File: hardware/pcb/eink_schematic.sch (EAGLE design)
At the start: 0 parts

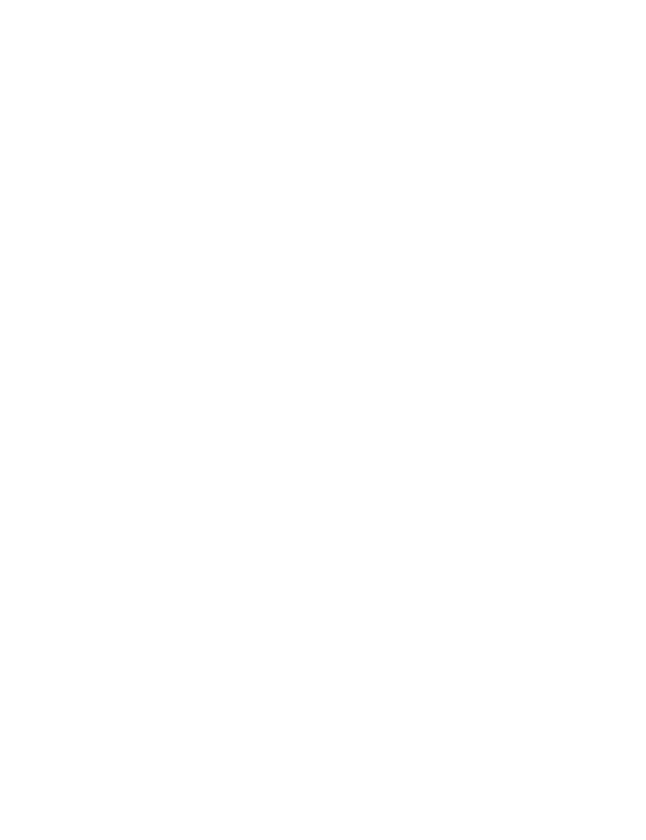
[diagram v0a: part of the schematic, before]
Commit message: rev78: just try writing text
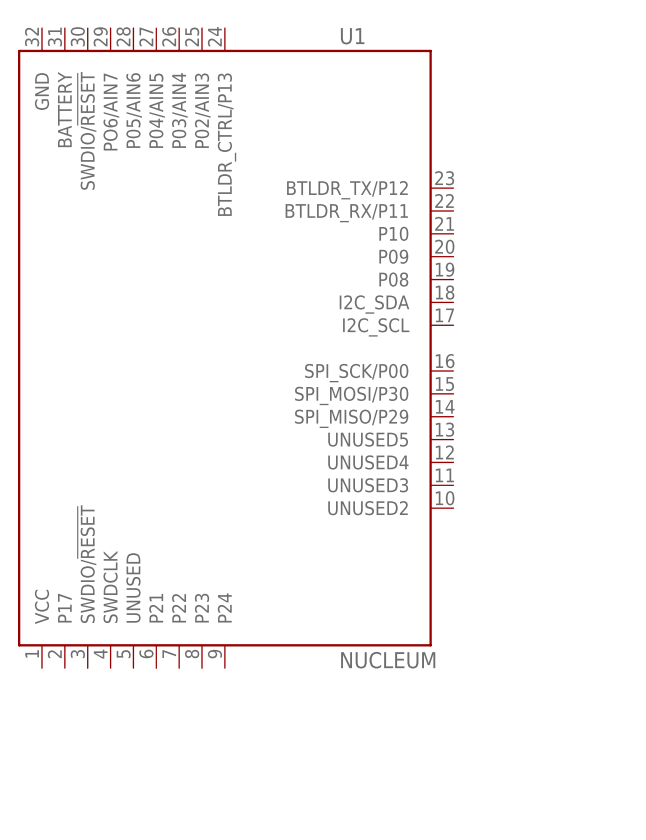
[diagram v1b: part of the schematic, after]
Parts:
- added U1: NUCLEUM, nucleum:NUCLEUM
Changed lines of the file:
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@@
 <parts>
 <part name="FRAME1" library="frames" deviceset="LETTER_L" device=""/>
+<part name="U1" library="nucleum" deviceset="NUCLEUM" device=""/>
 </parts>
 <sheets>
@@
 <instance part="FRAME1" gate="G$1" x="0" y="0"/>
 <instance part="FRAME1" gate="G$2" x="147.32" y="0"/>
+<instance part="U1" gate="G$1" x="127" y="101.6"/>
 </instances>
 <busses>

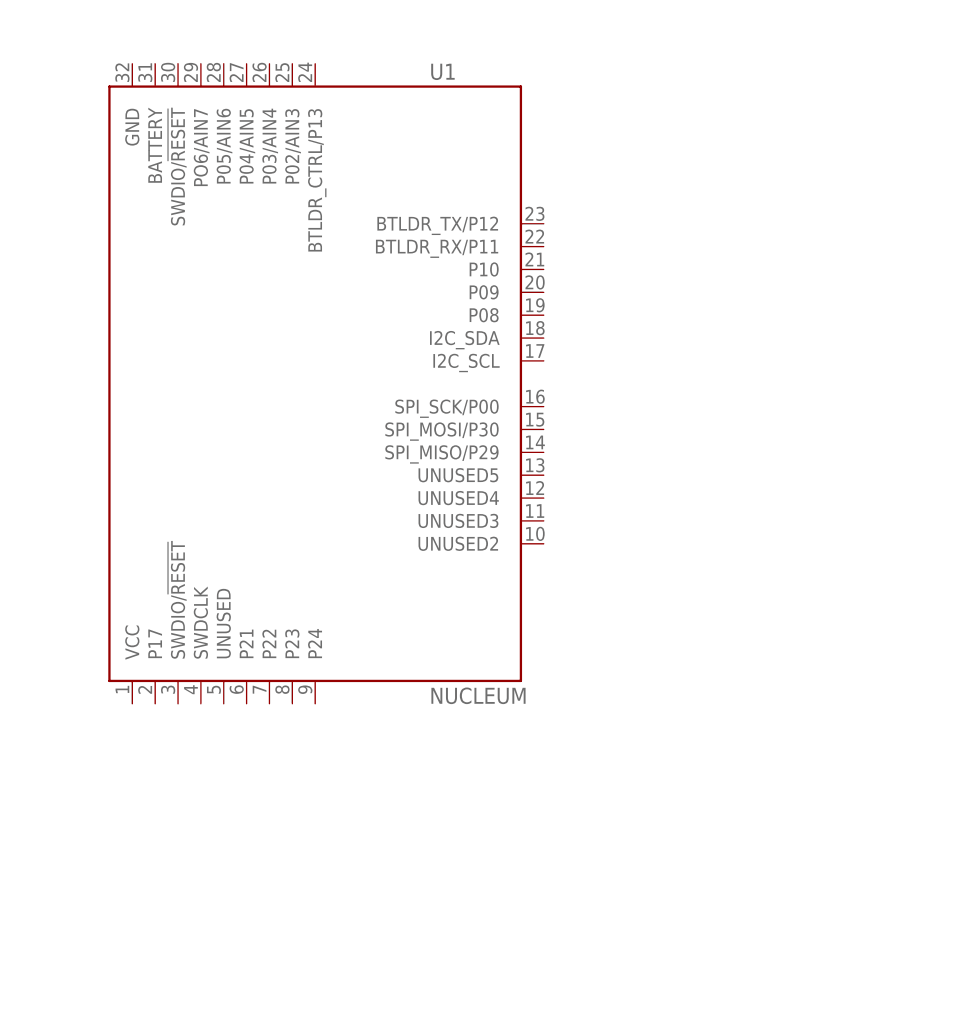
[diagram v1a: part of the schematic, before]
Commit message: Eagle: labeled B3-5 and SPI pins
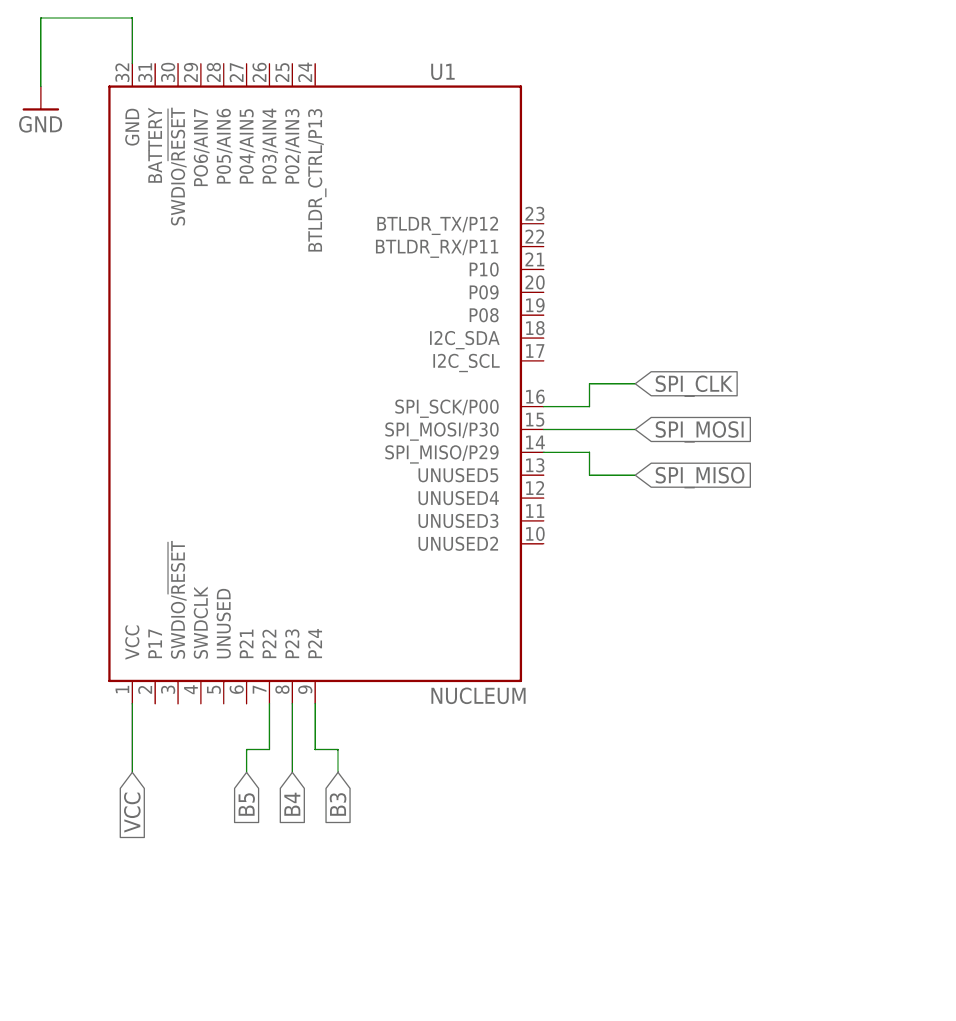
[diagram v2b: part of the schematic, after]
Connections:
- new net B3: U1.P24
- new net B4: U1.P23
- new net B5: U1.P22
- new net GND: U1.GND
- new net SPI_CLK: U1.SPI_SCK/P00
- new net SPI_MISO: U1.SPI_MISO/P29
- new net SPI_MOSI: U1.SPI_MOSI/P30
- new net VCC: U1.VCC
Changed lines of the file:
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@@
 <part name="FRAME1" library="frames" deviceset="LETTER_L" device=""/>
 <part name="U1" library="nucleum" deviceset="NUCLEUM" device=""/>
+<part name="GND1" library="umich" deviceset="GND" device=""/>
 </parts>
 <sheets>
@@
 <instance part="FRAME1" gate="G$2" x="147.32" y="0"/>
 <instance part="U1" gate="G$1" x="127" y="101.6"/>
+<instance part="GND1" gate="1" x="91.44" y="132.08"/>
 </instances>
 <busses>
 </busses>
 <nets>
+<net name="B4" class="0">
+<segment>
+<pinref part="U1" gate="G$1" pin="P23"/>
+<wire x1="119.38" y1="66.04" x2="119.38" y2="58.42" width="0.1524" layer="91"/>
+<label x="119.38" y="58.42" size="1.778" layer="95" rot="R270" xref="yes"/>
+</segment>
+</net>
+<net name="B3" class="0">
+<segment>
+<pinref part="U1" gate="G$1" pin="P24"/>
+<wire x1="121.92" y1="66.04" x2="121.92" y2="60.96" width="0.1524" layer="91"/>
+<wire x1="121.92" y1="60.96" x2="124.46" y2="60.96" width="0.1524" layer="91"/>
+<wire x1="124.46" y1="60.96" x2="124.46" y2="58.42" width="0.1524" layer="91"/>
+<label x="124.46" y="58.42" size="1.778" layer="95" rot="R270" xref="yes"/>
+</segment>
+</net>
+<net name="B5" class="0">
+<segment>
+<pinref part="U1" gate="G$1" pin="P22"/>
+<wire x1="116.84" y1="66.04" x2="116.84" y2="60.96" width="0.1524" layer="91"/>
+<wire x1="116.84" y1="60.96" x2="114.3" y2="60.96" width="0.1524" layer="91"/>
+<wire x1="114.3" y1="60.96" x2="114.3" y2="58.42" width="0.1524" layer="91"/>
+<label x="114.3" y="58.42" size="1.778" layer="95" rot="R270" xref="yes"/>
+</segment>
+</net>
+<net name="SPI_MOSI" class="0">
+<segment>
+<pinref part="U1" gate="G$1" pin="SPI_MOSI/P30"/>
+<wire x1="147.32" y1="96.52" x2="157.48" y2="96.52" width="0.1524" layer="91"/>
+<label x="157.48" y="96.52" size="1.778" layer="95" xref="yes"/>
+</segment>
+</net>
+<net name="SPI_CLK" class="0">
+<segment>
+<pinref part="U1" gate="G$1" pin="SPI_SCK/P00"/>
+<wire x1="147.32" y1="99.06" x2="152.4" y2="99.06" width="0.1524" layer="91"/>
+<wire x1="152.4" y1="99.06" x2="152.4" y2="101.6" width="0.1524" layer="91"/>
+<wire x1="152.4" y1="101.6" x2="157.48" y2="101.6" width="0.1524" layer="91"/>
+<label x="157.48" y="101.6" size="1.778" layer="95" xref="yes"/>
+</segment>
+</net>
+<net name="SPI_MISO" class="0">
+<segment>
+<pinref part="U1" gate="G$1" pin="SPI_MISO/P29"/>
+<wire x1="147.32" y1="93.98" x2="152.4" y2="93.98" width="0.1524" layer="91"/>
+<wire x1="152.4" y1="93.98" x2="152.4" y2="91.44" width="0.1524" layer="91"/>
+<wire x1="152.4" y1="91.44" x2="157.48" y2="91.44" width="0.1524" layer="91"/>
+<label x="157.48" y="91.44" size="1.778" layer="95" xref="yes"/>
+</segment>
+</net>
+<net name="GND" class="0">
+<segment>
+<pinref part="U1" gate="G$1" pin="GND"/>
+<wire x1="101.6" y1="137.16" x2="101.6" y2="142.24" width="0.1524" layer="91"/>
+<wire x1="101.6" y1="142.24" x2="91.44" y2="142.24" width="0.1524" layer="91"/>
+<wire x1="91.44" y1="142.24" x2="91.44" y2="134.62" width="0.1524" layer="91"/>
+<pinref part="GND1" gate="1" pin="GND"/>
+</segment>
+</net>
+<net name="VCC" class="0">
+<segment>
+<pinref part="U1" gate="G$1" pin="VCC"/>
+<wire x1="101.6" y1="66.04" x2="101.6" y2="58.42" width="0.1524" layer="91"/>
+<label x="101.6" y="58.42" size="1.778" layer="95" rot="R270" xref="yes"/>
+</segment>
+</net>
 </nets>
 </sheet>

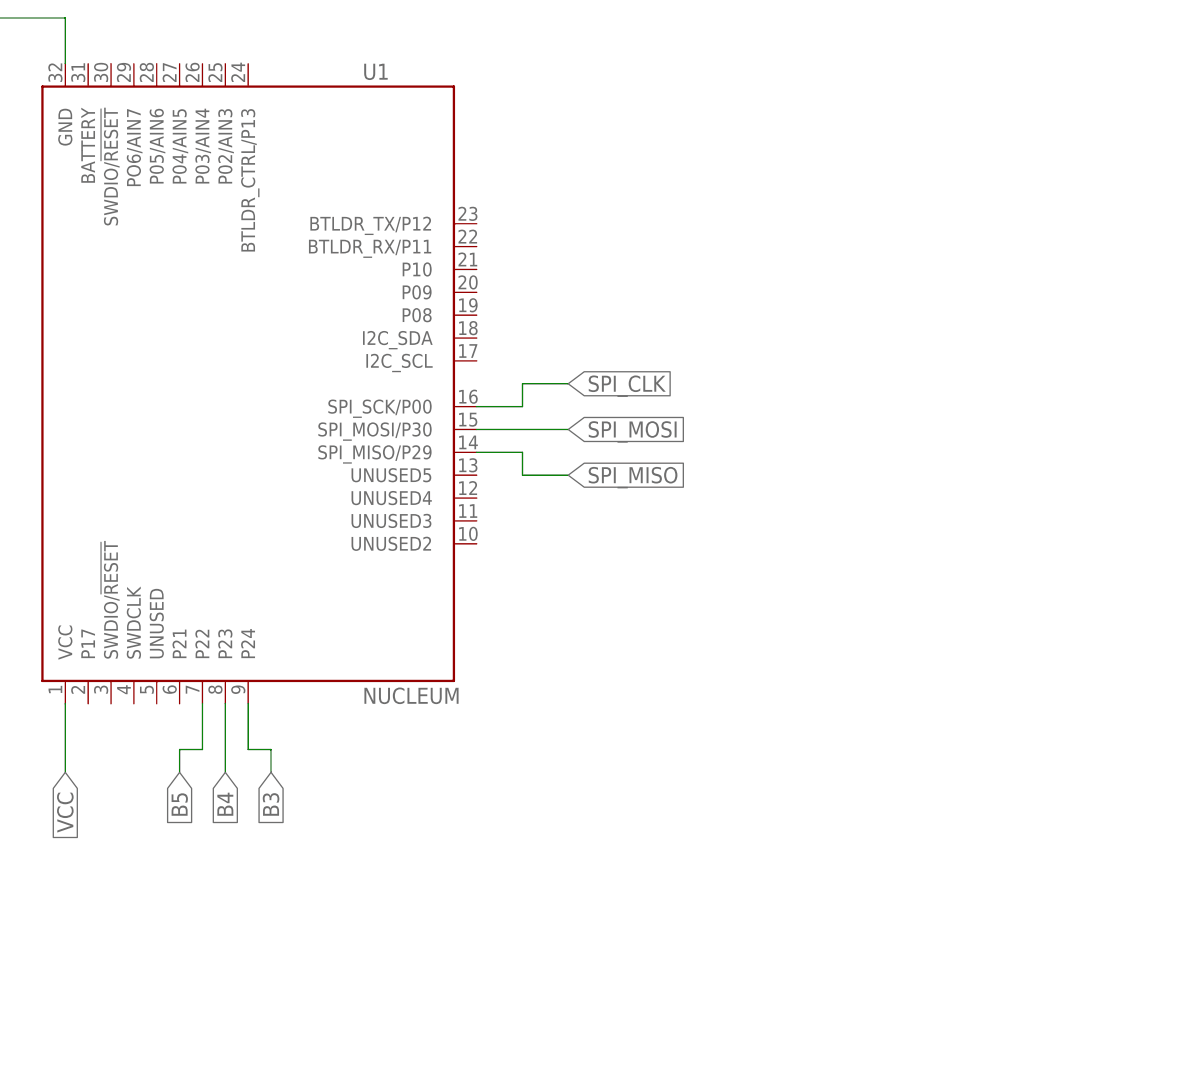
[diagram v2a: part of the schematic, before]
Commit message: Eagle: Added headers and labeled more
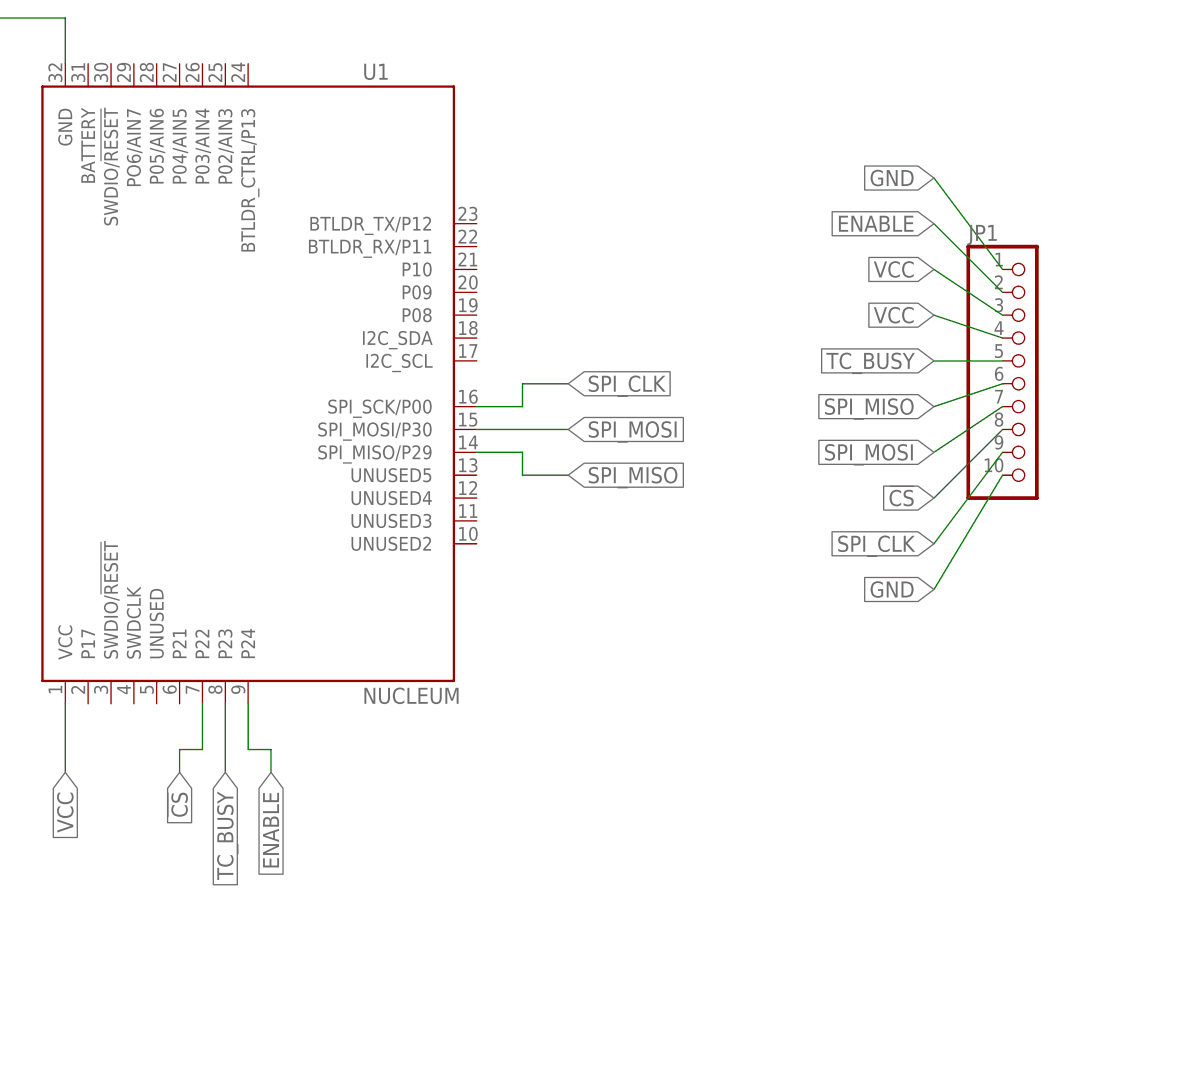
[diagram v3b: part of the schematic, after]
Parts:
- added JP1: (no value), pinhead:PINHD-1X10/90
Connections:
- removed net B3: U1.P24
- removed net B4: U1.P23
- removed net B5: U1.P22
- new net !CS: JP1.8, U1.P22
- new net ENABLE: JP1.2, U1.P24
- new net TC_BUSY: JP1.5, U1.P23
- net GND: now also JP1.1, JP1.10
- net SPI_CLK: now also JP1.9
- net SPI_MISO: now also JP1.6
- net SPI_MOSI: now also JP1.7
- net VCC: now also JP1.3, JP1.4
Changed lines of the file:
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@@
 <part name="U1" library="nucleum" deviceset="NUCLEUM" device=""/>
 <part name="GND1" library="umich" deviceset="GND" device=""/>
+<part name="JP1" library="pinhead" deviceset="PINHD-1X10" device="/90"/>
 </parts>
 <sheets>
@@
 <instance part="U1" gate="G$1" x="127" y="101.6"/>
 <instance part="GND1" gate="1" x="91.44" y="132.08"/>
+<instance part="JP1" gate="A" x="208.28" y="104.14"/>
 </instances>
 <busses>
 </busses>
 <nets>
-<net name="B4" class="0">
+<net name="TC_BUSY" class="0">
 <segment>
 <pinref part="U1" gate="G$1" pin="P23"/>
@@
 <label x="119.38" y="58.42" size="1.778" layer="95" rot="R270" xref="yes"/>
 </segment>
+<segment>
+<pinref part="JP1" gate="A" pin="5"/>
+<wire x1="205.74" y1="104.14" x2="198.12" y2="104.14" width="0.1524" layer="91"/>
+<label x="198.12" y="104.14" size="1.778" layer="95" rot="R180" xref="yes"/>
+</segment>
 </net>
-<net name="B3" class="0">
+<net name="ENABLE" class="0">
 <segment>
 <pinref part="U1" gate="G$1" pin="P24"/>
@@
 <label x="124.46" y="58.42" size="1.778" layer="95" rot="R270" xref="yes"/>
 </segment>
+<segment>
+<pinref part="JP1" gate="A" pin="2"/>
+<wire x1="205.74" y1="111.76" x2="198.12" y2="119.38" width="0.1524" layer="91"/>
+<label x="198.12" y="119.38" size="1.778" layer="95" rot="R180" xref="yes"/>
+</segment>
 </net>
-<net name="B5" class="0">
+<net name="!CS" class="0">
 <segment>
 <pinref part="U1" gate="G$1" pin="P22"/>
@@
 <label x="114.3" y="58.42" size="1.778" layer="95" rot="R270" xref="yes"/>
 </segment>
+<segment>
+<pinref part="JP1" gate="A" pin="8"/>
+<wire x1="205.74" y1="96.52" x2="198.12" y2="88.9" width="0.1524" layer="91"/>
+<label x="198.12" y="88.9" size="1.778" layer="95" rot="R180" xref="yes"/>
+</segment>
 </net>
 <net name="SPI_MOSI" class="0">
@@
 <wire x1="147.32" y1="96.52" x2="157.48" y2="96.52" width="0.1524" layer="91"/>
 <label x="157.48" y="96.52" size="1.778" layer="95" xref="yes"/>
+</segment>
+<segment>
+<pinref part="JP1" gate="A" pin="7"/>
+<wire x1="205.74" y1="99.06" x2="198.12" y2="93.98" width="0.1524" layer="91"/>
+<label x="198.12" y="93.98" size="1.778" layer="95" rot="R180" xref="yes"/>
 </segment>
 </net>
@@
 <label x="157.48" y="101.6" size="1.778" layer="95" xref="yes"/>
 </segment>
+<segment>
+<pinref part="JP1" gate="A" pin="9"/>
+<wire x1="205.74" y1="93.98" x2="198.12" y2="83.82" width="0.1524" layer="91"/>
+<label x="198.12" y="83.82" size="1.778" layer="95" rot="R180" xref="yes"/>
+</segment>
 </net>
 <net name="SPI_MISO" class="0">
@@
 <wire x1="152.4" y1="91.44" x2="157.48" y2="91.44" width="0.1524" layer="91"/>
 <label x="157.48" y="91.44" size="1.778" layer="95" xref="yes"/>
+</segment>
+<segment>
+<pinref part="JP1" gate="A" pin="6"/>
+<wire x1="205.74" y1="101.6" x2="198.12" y2="99.06" width="0.1524" layer="91"/>
+<label x="198.12" y="99.06" size="1.778" layer="95" rot="R180" xref="yes"/>
 </segment>
 </net>
@@
 <pinref part="GND1" gate="1" pin="GND"/>
 </segment>
+<segment>
+<pinref part="JP1" gate="A" pin="1"/>
+<wire x1="205.74" y1="114.3" x2="198.12" y2="124.46" width="0.1524" layer="91"/>
+<label x="198.12" y="124.46" size="1.778" layer="95" rot="R180" xref="yes"/>
+</segment>
+<segment>
+<pinref part="JP1" gate="A" pin="10"/>
+<wire x1="205.74" y1="91.44" x2="198.12" y2="78.74" width="0.1524" layer="91"/>
+<label x="198.12" y="78.74" size="1.778" layer="95" rot="R180" xref="yes"/>
+</segment>
 </net>
 <net name="VCC" class="0">
@@
 <label x="101.6" y="58.42" size="1.778" layer="95" rot="R270" xref="yes"/>
 </segment>
+<segment>
+<pinref part="JP1" gate="A" pin="3"/>
+<wire x1="205.74" y1="109.22" x2="198.12" y2="114.3" width="0.1524" layer="91"/>
+<label x="198.12" y="114.3" size="1.778" layer="95" rot="R180" xref="yes"/>
+</segment>
+<segment>
+<pinref part="JP1" gate="A" pin="4"/>
+<wire x1="205.74" y1="106.68" x2="198.12" y2="109.22" width="0.1524" layer="91"/>
+<label x="198.12" y="109.22" size="1.778" layer="95" rot="R180" xref="yes"/>
+</segment>
 </net>
